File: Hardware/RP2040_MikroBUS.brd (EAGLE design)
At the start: 30.5 x 91.4 mm, 136 parts, among them J1 SWD, J3 Qwiic, J5 USB C, J6 microSD, Q1 20V/4.2A/52mΩ/1.4W, U2 MAX17048, U3 MCP73831, U4 W25QXX128MBIT, U5 RP2040, U6 WS2812-2020, U7 3.3V, Y2 12MHz

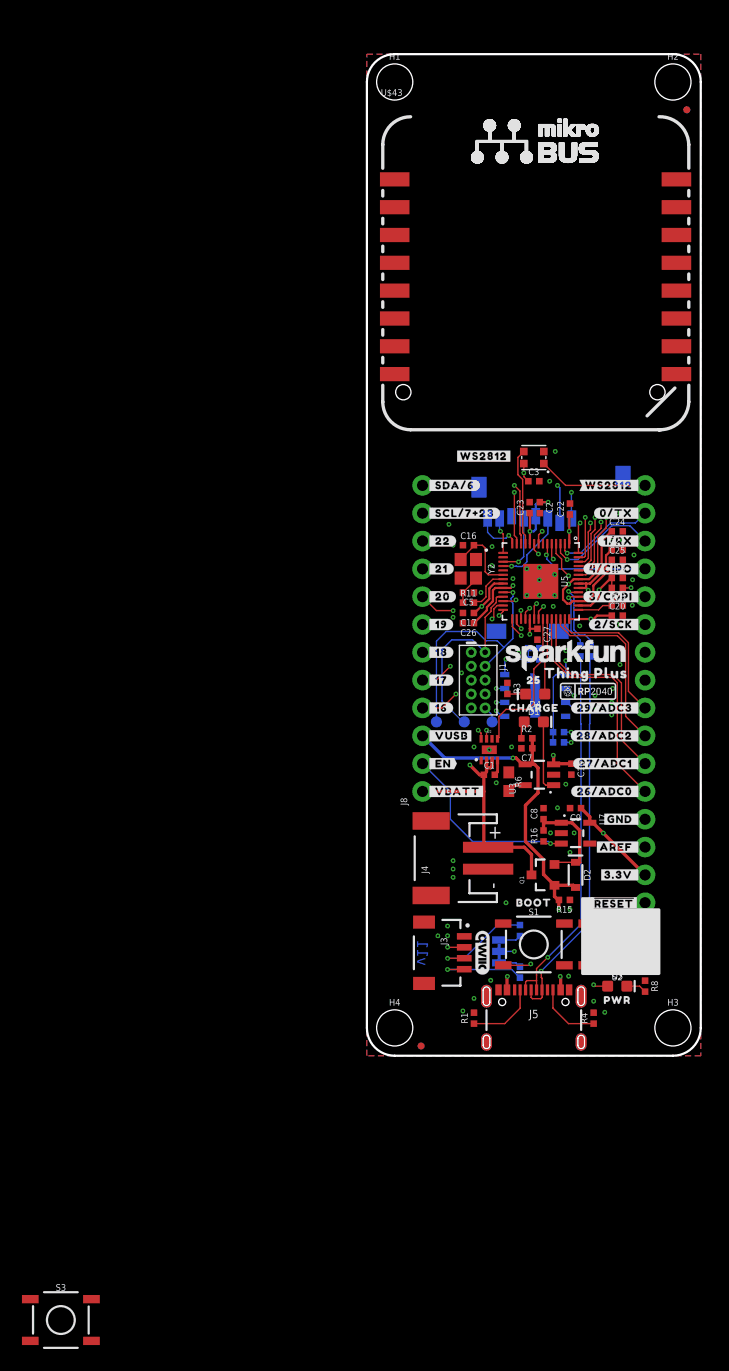
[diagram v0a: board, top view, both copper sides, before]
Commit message: Rename eagle files
Make sure everything is connected in the schematic
Parts are laid out where they should be on board, need to just route/re-route.
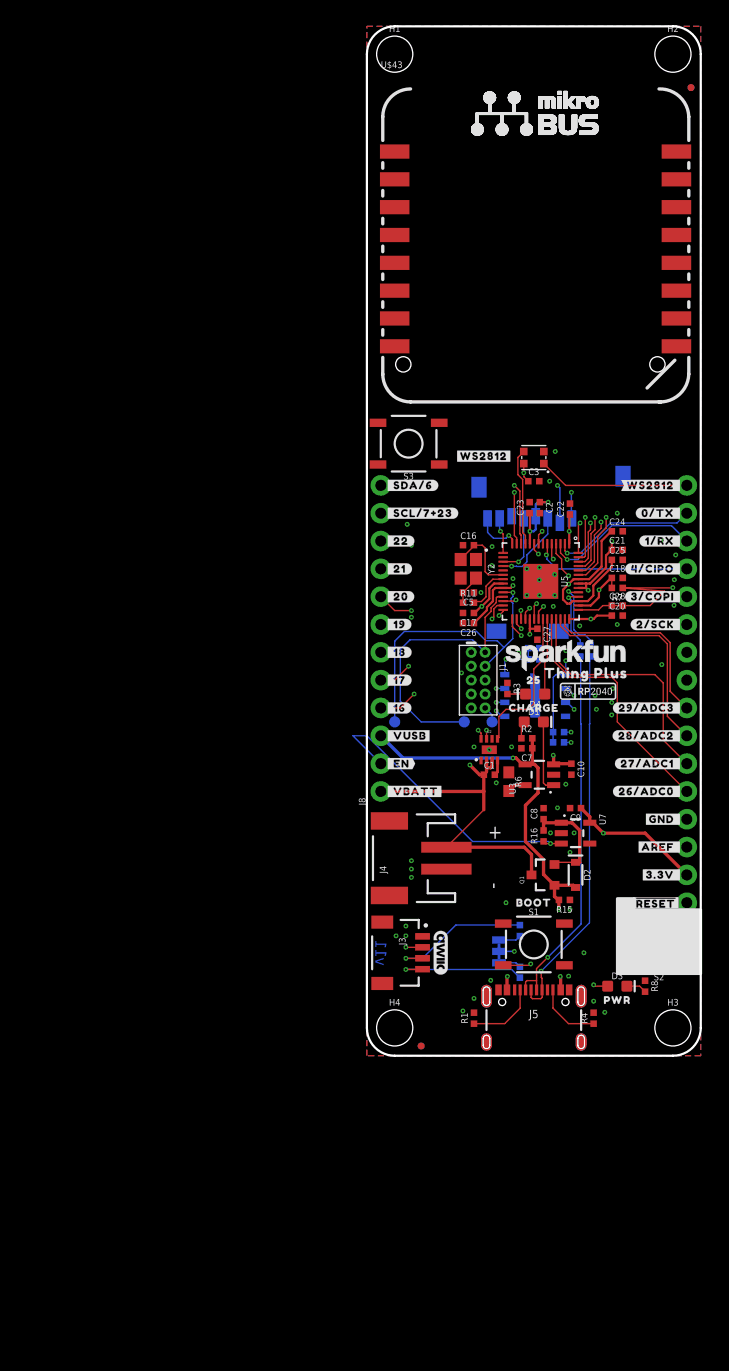
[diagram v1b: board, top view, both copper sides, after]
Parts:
- moved S3 86.1 mm to (3.81, 55.9), turned to 180 degrees
- moved J7 3.81 mm to (29.2, 14.0)
- moved S2 3.81 mm to (26.7, 10.2)
- moved U$10 3.81 mm to (28.8, 52.1)
- moved U$11 3.81 mm to (28.8, 49.5)
- moved U$12 3.81 mm to (28.8, 47.0)
- moved U$13 3.81 mm to (28.8, 44.5)
- moved U$14 3.81 mm to (28.8, 41.9)
- moved U$15 3.81 mm to (28.8, 39.4)
- moved U$18 3.81 mm to (28.8, 31.8)
- moved U$19 3.81 mm to (28.8, 29.2)
- moved U$20 3.81 mm to (28.8, 26.7)
- moved U$21 3.81 mm to (28.8, 24.1)
- moved U$25 3.81 mm to (28.8, 21.6)
- moved U$26 3.81 mm to (28.8, 19.1)
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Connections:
- removed net N$20: U$43.3
- removed net N$24: U$43.16
- removed net N$25: U$43.15
- new net SPI0_CS: U$43.3, U5.7
- net GPIO16: now also U$43.16
- net GPIO17: now also U$43.15
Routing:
- net I2C1_SCL/GPIO23: track 75.2 -> 88.2 mm
- net I2C1_SDA: track 72.7 -> 85.7 mm
- net AVDD: track 30.5 -> 41.5 mm
- net EN: track 17.9 -> 27.4 mm
- net V_BATT: track 34.8 -> 43.7 mm
- net SWDIO: track 18.4 -> 26.0 mm
- net ADC2: track 16.4 -> 20.2 mm
- net SPI0_SCK: track 12.2 -> 16.0 mm
- net WS2812_DO: track 10.1 -> 13.9 mm
- net V_USB: track 44.5 -> 48.3 mm
- net UART0_TX: track 9.57 -> 13.4 mm
- net SWDCK: track 23.3 -> 27.1 mm
- net SPI0_COPI: track 11.3 -> 15.1 mm
- net SPI0_CIPO: track 10.8 -> 14.6 mm
- net GPIO18: track 11.8 -> 15.6 mm
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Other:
- board size 30.5 x 91.4 mm -> 30.5 x 94 mm

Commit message: Routing finished!
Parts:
- TP1, TP2, TP3: value (none) -> TEST-POINT3X4
- moved J6 39.5 mm to (8.26, 77.9)
- moved S3 0.81 mm to (4.45, 56.4)
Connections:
- net !RESET!: now also TP3.1; no longer TP3.P$1
- net SWDCK: now also TP1.1; no longer TP1.P$1
- net SWDIO: now also TP2.1; no longer TP2.P$1
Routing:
- net ADC0: track 23.1 -> 107.5 mm, vias 0 -> 2
- net GPIO16: track 18.7 -> 93.3 mm, vias 2 -> 4
- net GPIO17: track 15.9 -> 76.3 mm, vias 2 -> 3
- net SPI0_SCK: track 16.0 -> 75.8 mm, vias 1 -> 2
- net V_USB: track 48.3 -> 106.9 mm, vias 4 -> 6
- net I2C1_SCL/GPIO23: track 88.2 -> 139.4 mm, vias 5 -> 6
- net SPI0_COPI: track 15.1 -> 66.3 mm
- net SPI0_CIPO: track 14.6 -> 62.0 mm, vias 1 -> 2
- net SPI0_CS: track 0.00 -> 44.6 mm, vias 0 -> 2
- net SPI_SCK1/SDIO_CLK: track 5.58 -> 46.0 mm, vias 1 -> 2
- net SPI_CIPO1/SDIO_DAT0: track 3.28 -> 43.4 mm, vias 1 -> 2
- net SPI_COPI1/SDIO_CMD: track 7.12 -> 46.6 mm, vias 1 -> 2
- net SDIO_DAT1: track 4.42 -> 43.4 mm, vias 1 -> 2
- net I2C1_SDA: track 85.7 -> 121.5 mm, vias 3 -> 5
- net UART0_RX: track 14.5 -> 49.7 mm, vias 1 -> 3
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
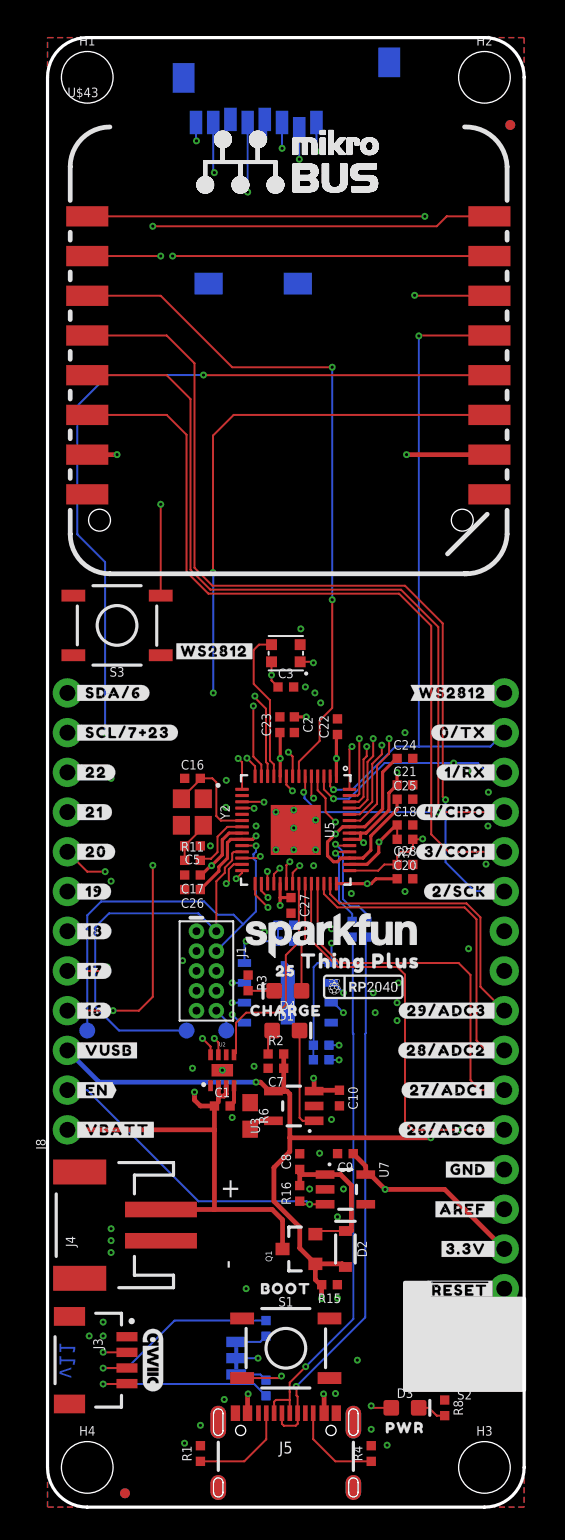
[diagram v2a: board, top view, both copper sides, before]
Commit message: Made board dimensions on grid
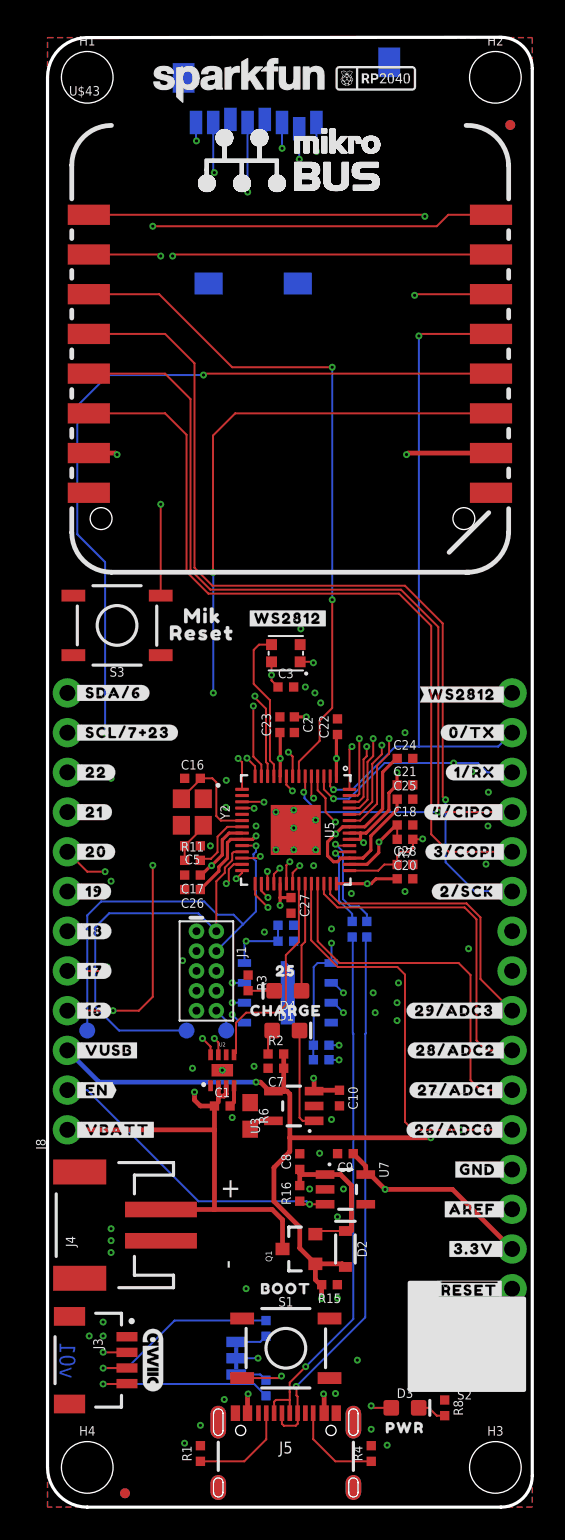
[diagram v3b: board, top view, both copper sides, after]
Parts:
- removed U$47: (no value), output:THING_PLUS_0
- added U$46: (no value), output:RESET0
- U$44: device output:THING_PLUS0 -> output:MIK0
- moved U$29 58.1 mm to (21.0, 91.4)
- moved U$45 55.0 mm to (12.3, 91.3)
- moved U$44 39.9 mm to (8.00, 57.0), flipped to the top
- moved U$60 5.15 mm to (15.4, 56.8)
- moved H2 0.70 mm to (28.6, 91.4)
- moved H3 0.70 mm to (28.6, 2.54)
- moved U$10 0.61 mm to (29.4, 52.0)
- moved U$11 0.60 mm to (29.4, 49.5)
- moved U$12 0.60 mm to (29.4, 47.0)
- moved U$14 0.60 mm to (29.4, 41.9)
- moved U$19 0.60 mm to (29.4, 29.2)
- moved U$25 0.60 mm to (29.4, 21.6)
- moved U$26 0.60 mm to (29.4, 19.1)
- moved U$28 0.60 mm to (29.3, 14.0)
- moved U$37 0.60 mm to (29.4, 19.1)
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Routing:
- net SPI0_COPI: track 66.3 -> 67.2 mm
- net SPI0_SCK: track 75.8 -> 76.7 mm
- net UART0_TX: track 44.2 -> 44.8 mm
- net UART0_RX: track 49.7 -> 50.3 mm
- net WS2812_DO: track 13.9 -> 14.4 mm
- net AVDD: track 34.5 -> 35.0 mm
- net ADC2: track 20.9 -> 21.4 mm
- net ADC1: track 23.5 -> 24.0 mm
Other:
- board size 30.5 x 94 mm -> 31 x 94 mm
- board text added: "v01"
- board text removed: "v11"

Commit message: Update RP2040_MikroBUS.brd
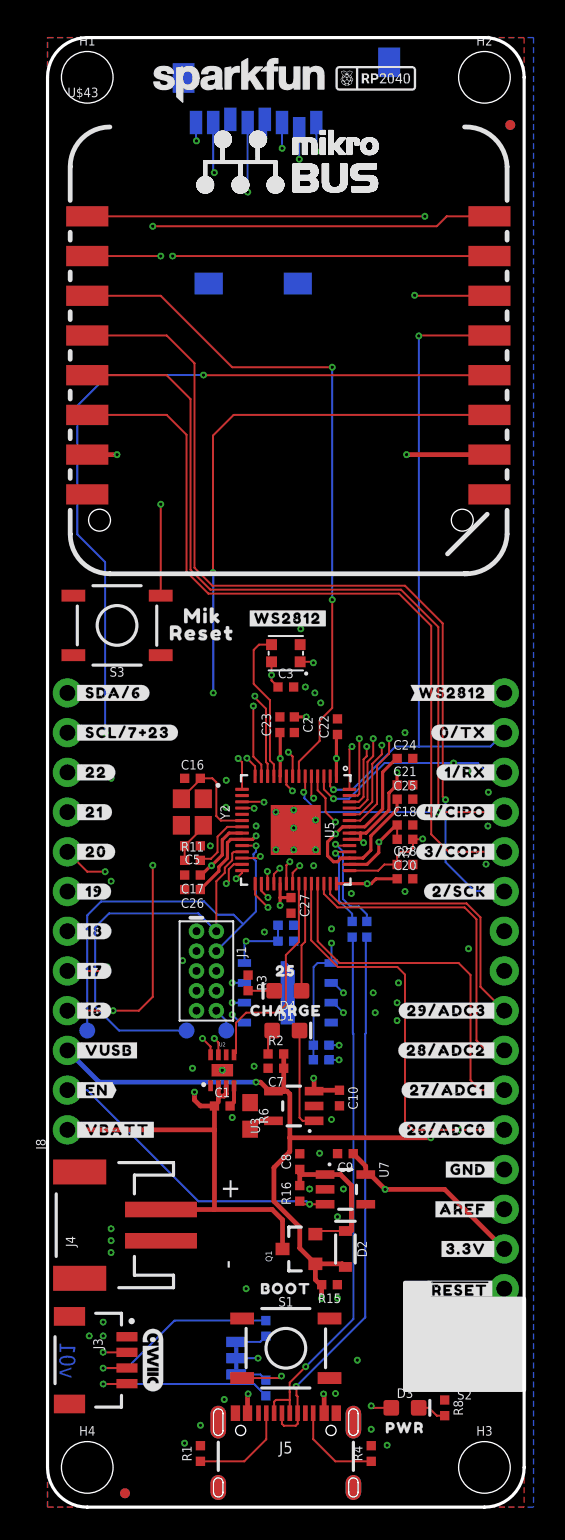
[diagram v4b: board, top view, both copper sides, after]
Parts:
- moved H2 0.70 mm to (27.9, 91.4)
- moved H3 0.70 mm to (27.9, 2.54)
- moved U$10 0.61 mm to (28.8, 52.1)
- moved U$11 0.60 mm to (28.8, 49.5)
- moved U$12 0.60 mm to (28.8, 47.0)
- moved U$14 0.60 mm to (28.8, 41.9)
- moved U$19 0.60 mm to (28.8, 29.2)
- moved U$25 0.60 mm to (28.8, 21.6)
- moved U$26 0.60 mm to (28.8, 19.1)
- moved U$28 0.60 mm to (28.7, 14.0)
- moved U$37 0.60 mm to (28.8, 19.1)
- moved U$38 0.60 mm to (28.8, 21.6)
- moved U$41 0.60 mm to (28.8, 29.2)
- moved J7 0.50 mm to (29.2, 14.0)
- moved U$13 0.50 mm to (28.8, 44.5)
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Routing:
- net SPI0_SCK: track 76.7 -> 75.8 mm
- net SPI0_COPI: track 67.2 -> 66.3 mm
- net UART0_TX: track 44.8 -> 44.2 mm
- net UART0_RX: track 50.3 -> 49.7 mm
- net WS2812_DO: track 14.4 -> 13.9 mm
- net AVDD: track 35.0 -> 34.5 mm
- net ADC2: track 21.4 -> 20.9 mm
- net ADC1: track 24.0 -> 23.5 mm
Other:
- board size 31 x 94 mm -> 30.5 x 94 mm

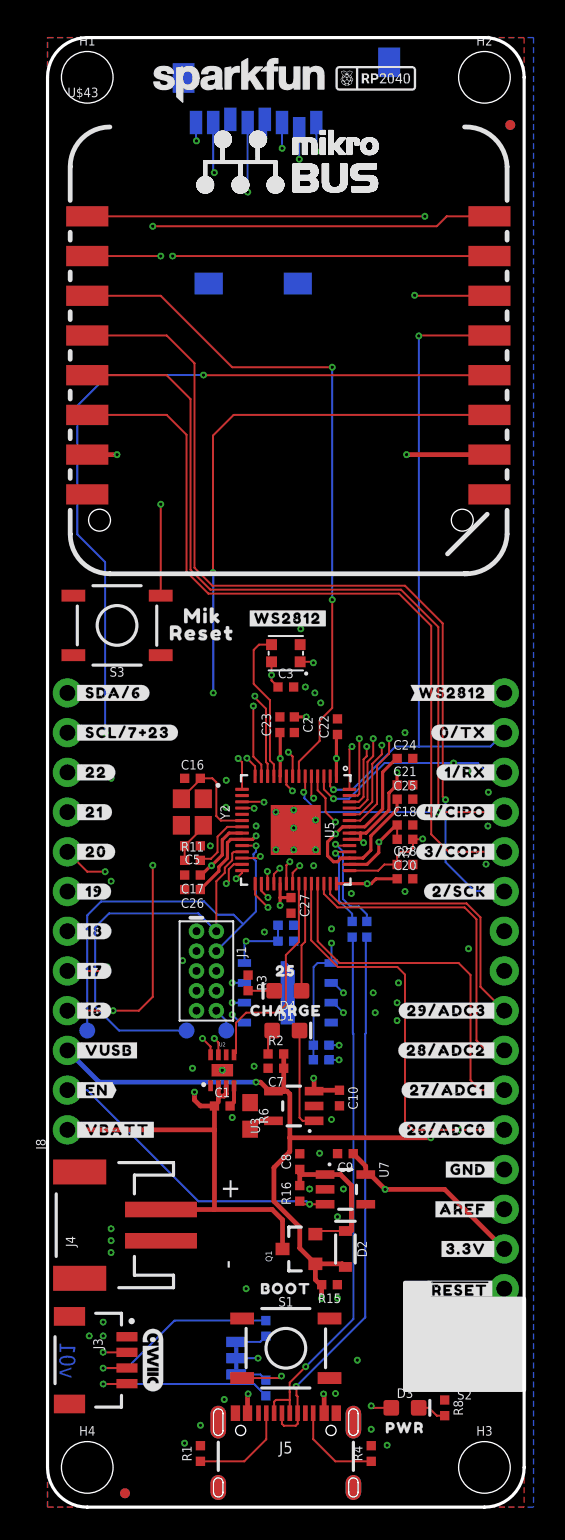
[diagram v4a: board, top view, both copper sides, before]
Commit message: Space pins for thing plus shields
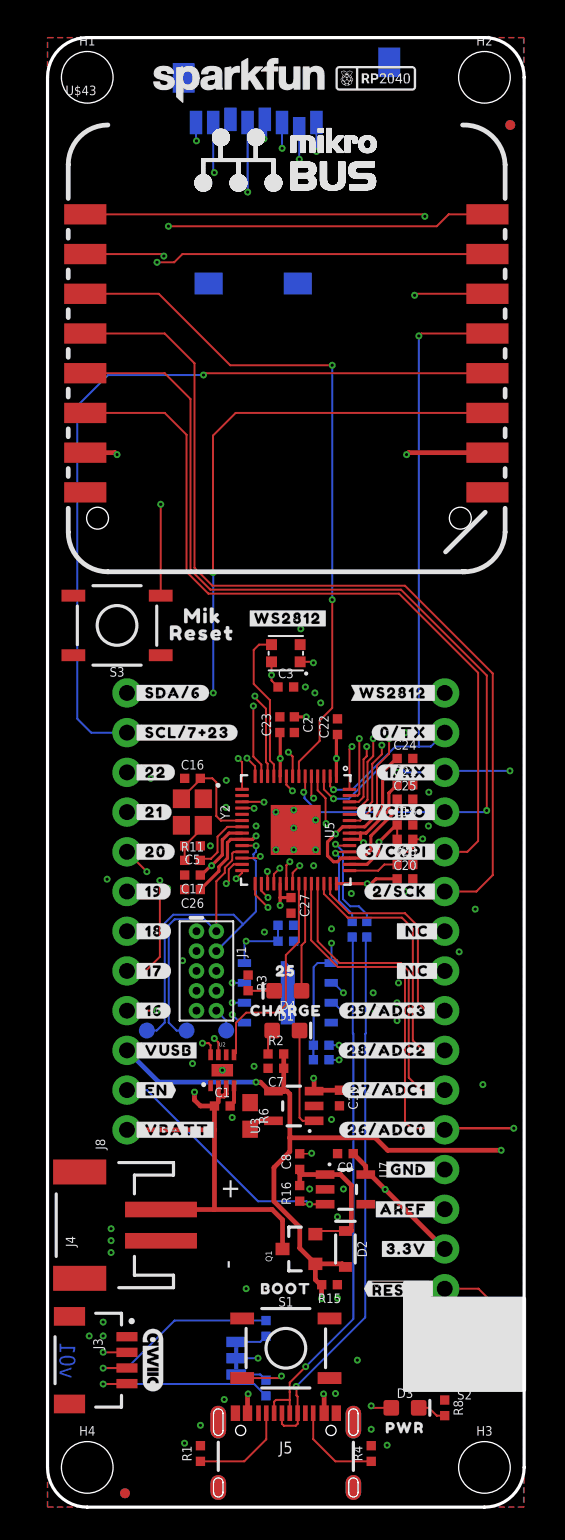
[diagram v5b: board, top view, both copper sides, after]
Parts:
- added U$47, U$48: (no value), output:#_NC_#0
- added U$49: (no value), output:#_2#SCK#0
- added U$50: (no value), output:#_3#COPI#0
- added U$51: (no value), output:#_4#CIPO#0
- added U$52: (no value), output:#_1#RX#0
- added U$53: (no value), output:#_0#TX#0
- added U$71: (no value), output:#_WS2812#0
- moved J7 3.81 mm to (25.4, 14.0)
- moved U$10 3.81 mm to (25.0, 52.1)
- moved U$11 3.81 mm to (25.0, 49.5)
- moved U$12 3.81 mm to (25.0, 47.0)
- moved U$13 3.81 mm to (25.0, 44.5)
- moved U$14 3.81 mm to (25.0, 41.9)
- moved U$15 3.81 mm to (25.0, 39.4)
- moved U$18 3.81 mm to (25.0, 31.8)
- moved U$19 3.81 mm to (25.0, 29.2)
- moved U$20 3.81 mm to (25.0, 26.7)
- moved U$21 3.81 mm to (25.0, 24.1)
- moved U$25 3.81 mm to (25.0, 21.6)
- moved U$26 3.81 mm to (25.0, 19.1)
- moved U$27 3.81 mm to (25.0, 16.5)
- moved U$28 3.81 mm to (24.9, 14.0)
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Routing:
- net GPIO16: track 93.3 -> 79.1 mm
- net SWDIO: track 26.2 -> 17.2 mm
- net ADC0: track 107.5 -> 114.2 mm
- net SWDCK: track 27.1 -> 22.0 mm
- net SPI0_COPI: track 66.3 -> 61.6 mm
- net ADC2: track 20.9 -> 16.7 mm
- net SPI0_SCK: track 75.8 -> 71.8 mm, vias 2 -> 1
- net UART0_TX: track 44.2 -> 40.3 mm
- net AVDD: track 34.5 -> 30.7 mm
- net WS2812_DO: track 13.9 -> 10.1 mm
- net V_BATT: track 42.6 -> 38.8 mm
- net GPIO18: track 15.6 -> 11.8 mm
- net EN: track 20.2 -> 16.4 mm
- net GPIO20: track 14.1 -> 10.3 mm
- net GPIO19: track 14.0 -> 10.2 mm
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
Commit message: Design review
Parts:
- moved S2 3.81 mm to (22.9, 10.2)
- moved U$17 3.81 mm to (10.4, 9.53)
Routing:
- net !RESET!: track 49.9 -> 47.1 mm
- net I2C1_SDA: track 120.5 -> 122.1 mm
- net SPI_SCK1/SDIO_CLK: track 46.0 -> 45.0 mm, vias 2 -> 1
- net SDIO_DAT1: track 43.4 -> 44.0 mm, vias 2 -> 1
- net I2C1_SCL/GPIO23: track 139.8 -> 140.4 mm
- net SPI0_CIPO: track 62.2 -> 62.8 mm
- net SPI_COPI1/SDIO_CMD: vias 2 -> 1
- net SPI_CIPO1/SDIO_DAT0: vias 2 -> 1
- net SPI_!CS1!/SDIO_DAT3: vias 3 -> 2
- net SDIO_DAT2: vias 3 -> 2
